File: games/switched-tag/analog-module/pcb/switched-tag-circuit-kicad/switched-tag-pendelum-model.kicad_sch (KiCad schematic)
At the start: 7 parts

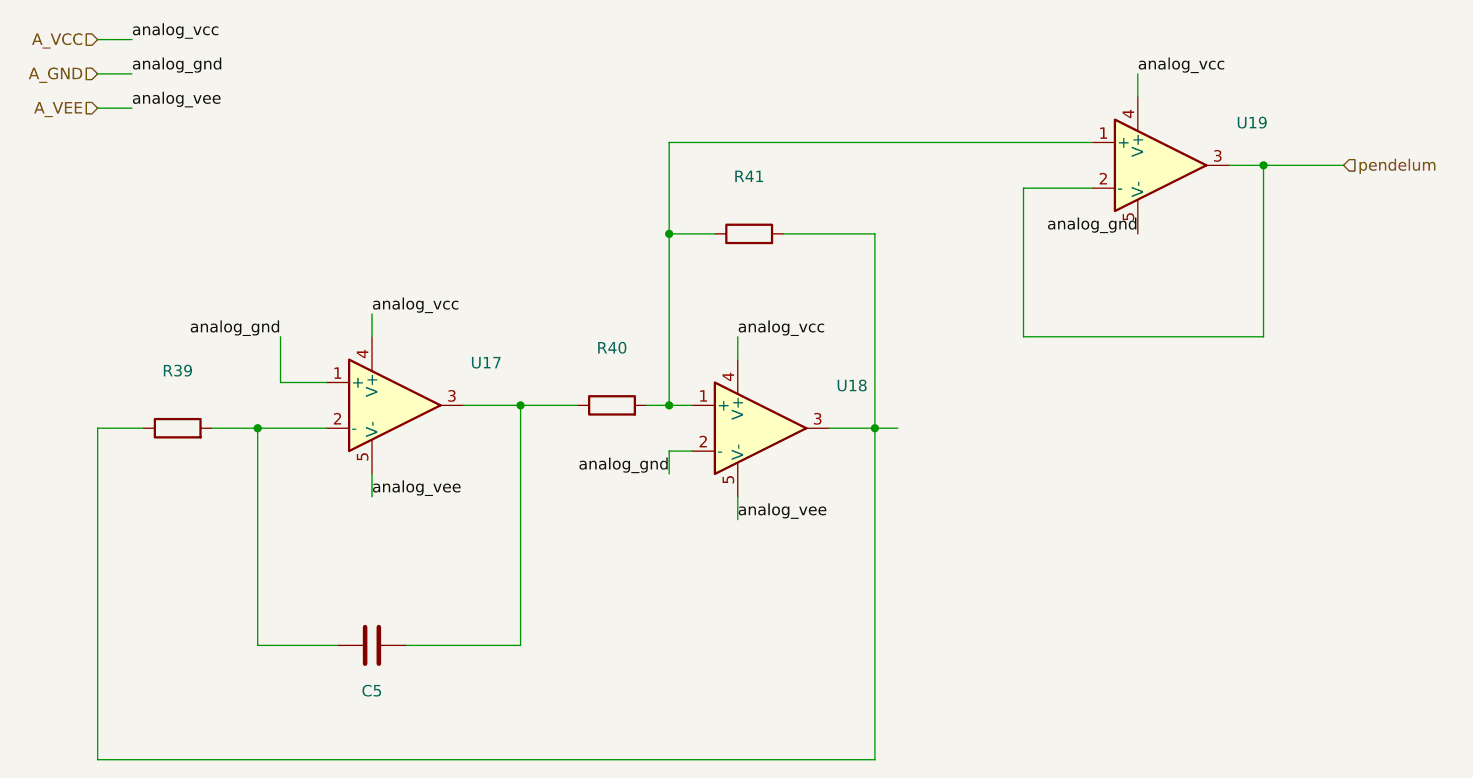
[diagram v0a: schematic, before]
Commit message: Converted Lm358.mod to .lib file for convenience.
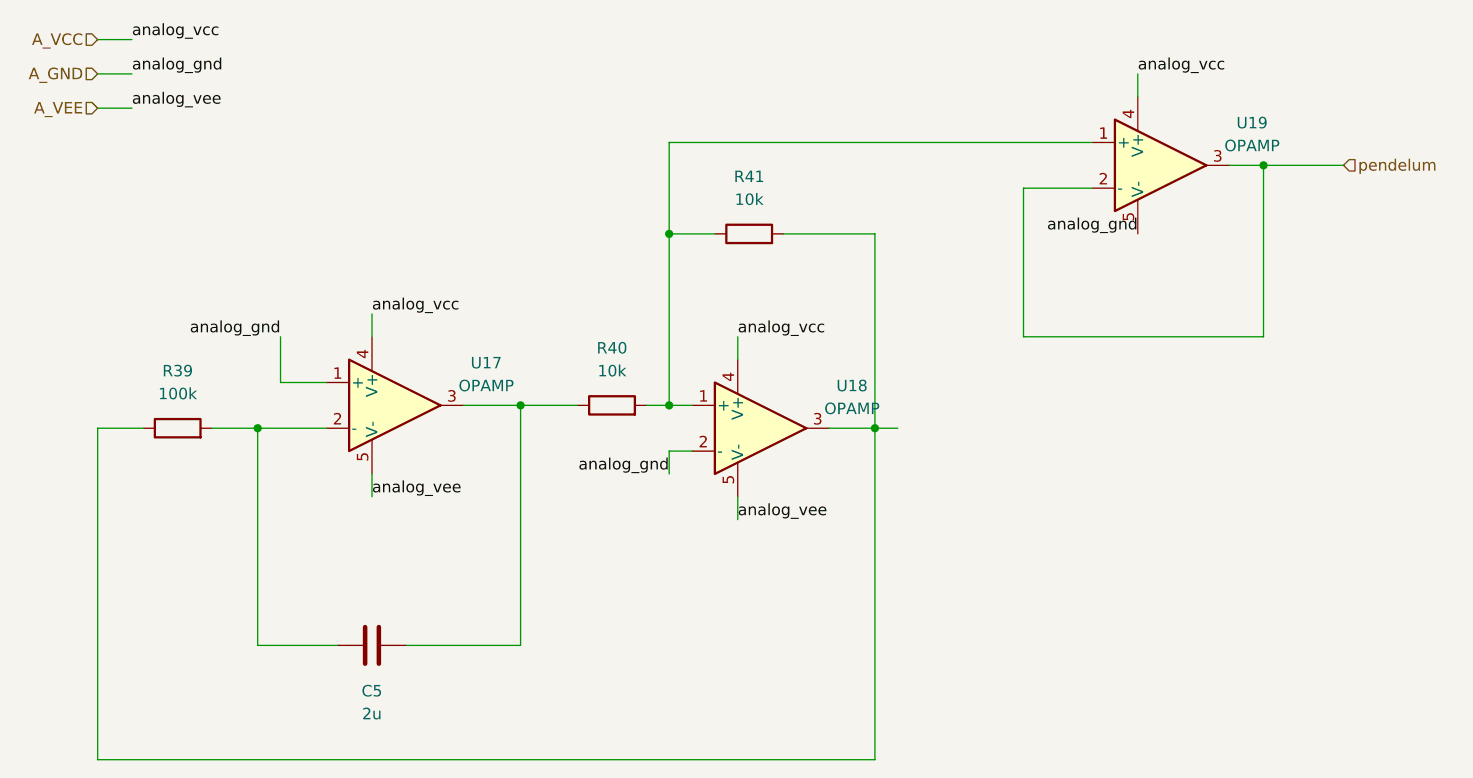
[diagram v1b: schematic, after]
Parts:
- C5: value (none) -> 2u
- R39: value (none) -> 100k
- R40, R41: value (none) -> 10k
- U17, U18, U19: value (none) -> OPAMP; Spice_Lib_File /home/pab/Inventions/analog-circuit-game-console/ms-circuit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 -> (none); Spice_Model AD8031 -> (none); Spice_Netlist_Enabled Y -> (none); Spice_Node_Sequence 1 2 4 5 3 -> (none); Spice_Primitive X -> (none)
